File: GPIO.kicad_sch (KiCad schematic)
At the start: 18 parts, among them J11 74LS245, J9 uPD446, K15 74LS04, U2 74LS10

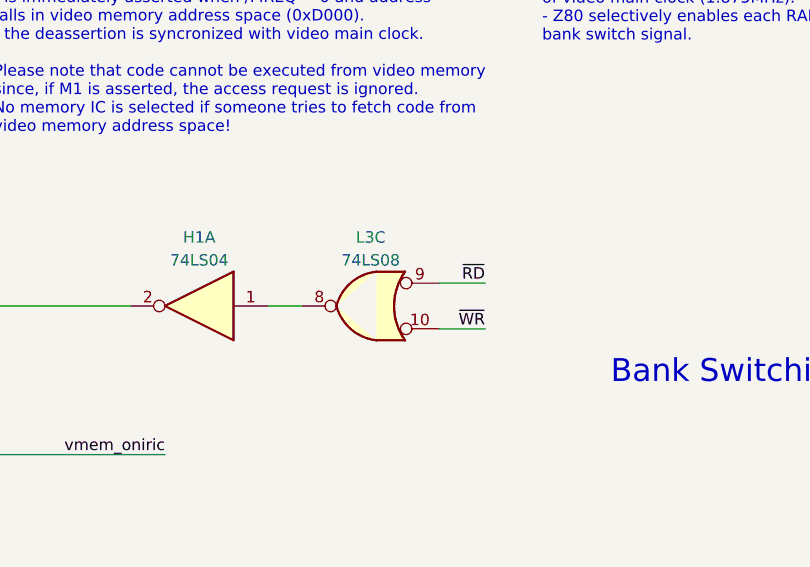
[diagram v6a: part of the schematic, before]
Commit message: IO addressing space multiplexing and small IO description
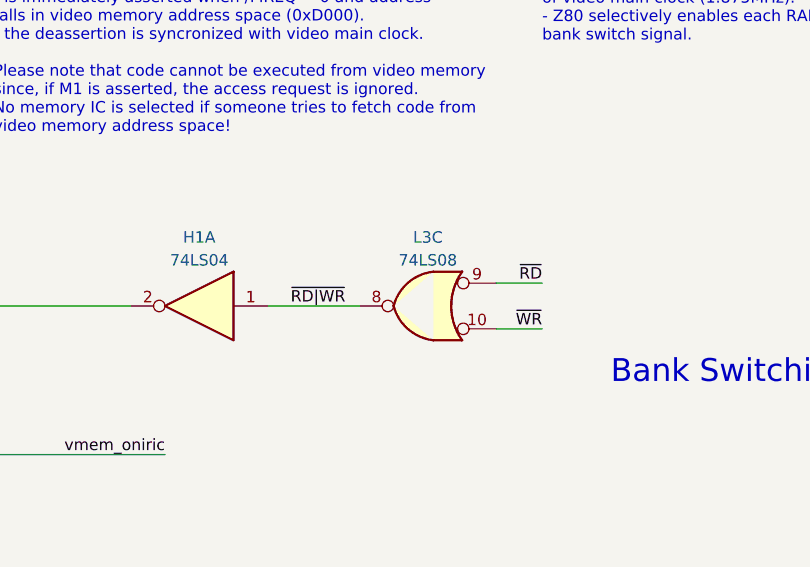
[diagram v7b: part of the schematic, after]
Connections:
- net ~{RD|WR}: now reaches H1.1, L3.8
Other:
- moved on the sheet: L3C
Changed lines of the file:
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@@
     (stroke (width 0) (type default))
   )
-  (wire (pts (xy 173.99 153.67) (xy 179.07 153.67))
+  (wire (pts (xy 180.34 153.67) (xy 185.42 153.67))
     (stroke (width 0) (type default))
   )
@@
     (stroke (width 0) (type default))
   )
-  (wire (pts (xy 173.99 148.59) (xy 179.07 148.59))
+  (wire (pts (xy 180.34 148.59) (xy 185.42 148.59))
     (stroke (width 0) (type default))
   )
@@
     (stroke (width 0) (type default))
   )
-  (wire (pts (xy 154.94 151.13) (xy 158.75 151.13))
+  (wire (pts (xy 154.94 151.13) (xy 165.1 151.13))
     (stroke (width 0) (type default))
   )
@@
     (effects (font (size 1.27 1.27)) (justify right bottom))
   )
-  (label "~{WR}" (at 179.07 153.67 180) (fields_autoplaced)
+  (label "~{WR}" (at 185.42 153.67 180) (fields_autoplaced)
     (effects (font (size 1.27 1.27)) (justify right bottom))
   )
@@
     (effects (font (size 1.27 1.27)) (justify left bottom))
   )
+  (label "~{RD|WR}" (at 157.48 151.13 0) (fields_autoplaced)
+    (effects (font (size 1.27 1.27)) (justify left bottom))
+  )
   (label "vmem_oniric" (at -19.05 274.32 0) (fields_autoplaced)
     (effects (font (size 1.27 1.27)) (justify left bottom))
@@
     (effects (font (size 1.27 1.27)) (justify left bottom))
   )
-  (label "~{RD}" (at 179.07 148.59 180) (fields_autoplaced)
+  (label "~{RD}" (at 185.42 148.59 180) (fields_autoplaced)
     (effects (font (size 1.27 1.27)) (justify right bottom))
   )
@@
     )
   )
-  (symbol (lib_id "74xx:74LS08") (at 166.37 151.13 0) (mirror y) (unit 3) (convert 2)
+  (symbol (lib_id "74xx:74LS08") (at 172.72 151.13 0) (mirror y) (unit 3) (convert 2)
     (in_bom yes) (on_board yes) (dnp no) (fields_autoplaced)
-    (property "Reference" "L3" (at 166.37 143.51 0)
+    (property "Reference" "L3" (at 172.72 143.51 0)
       (effects (font (size 1.27 1.27)))
     )
-    (property "Value" "74LS08" (at 166.37 146.05 0)
+    (property "Value" "74LS08" (at 172.72 146.05 0)
       (effects (font (size 1.27 1.27)))
     )
-    (property "Footprint" "" (at 166.37 151.13 0)
-      (effects (font (size 1.27 1.27)) hide)
-    )
-    (property "Datasheet" "http://www.ti.com/lit/gpn/sn74LS08" (at 166.37 151.13 0)
-      (effects (font (size 1.27 1.27)) hide)
-    )
+    (property "Footprint" "" (at 172.72 151.13 0)
+      (effects (font (size 1.27 1.27)) hide)
+    )
+    (property "Datasheet" "http://www.ti.com/lit/gpn/sn74LS08" (at 172.72 151.13 0)
+      (effects (font (size 1.27 1.27)) hide)
+    )

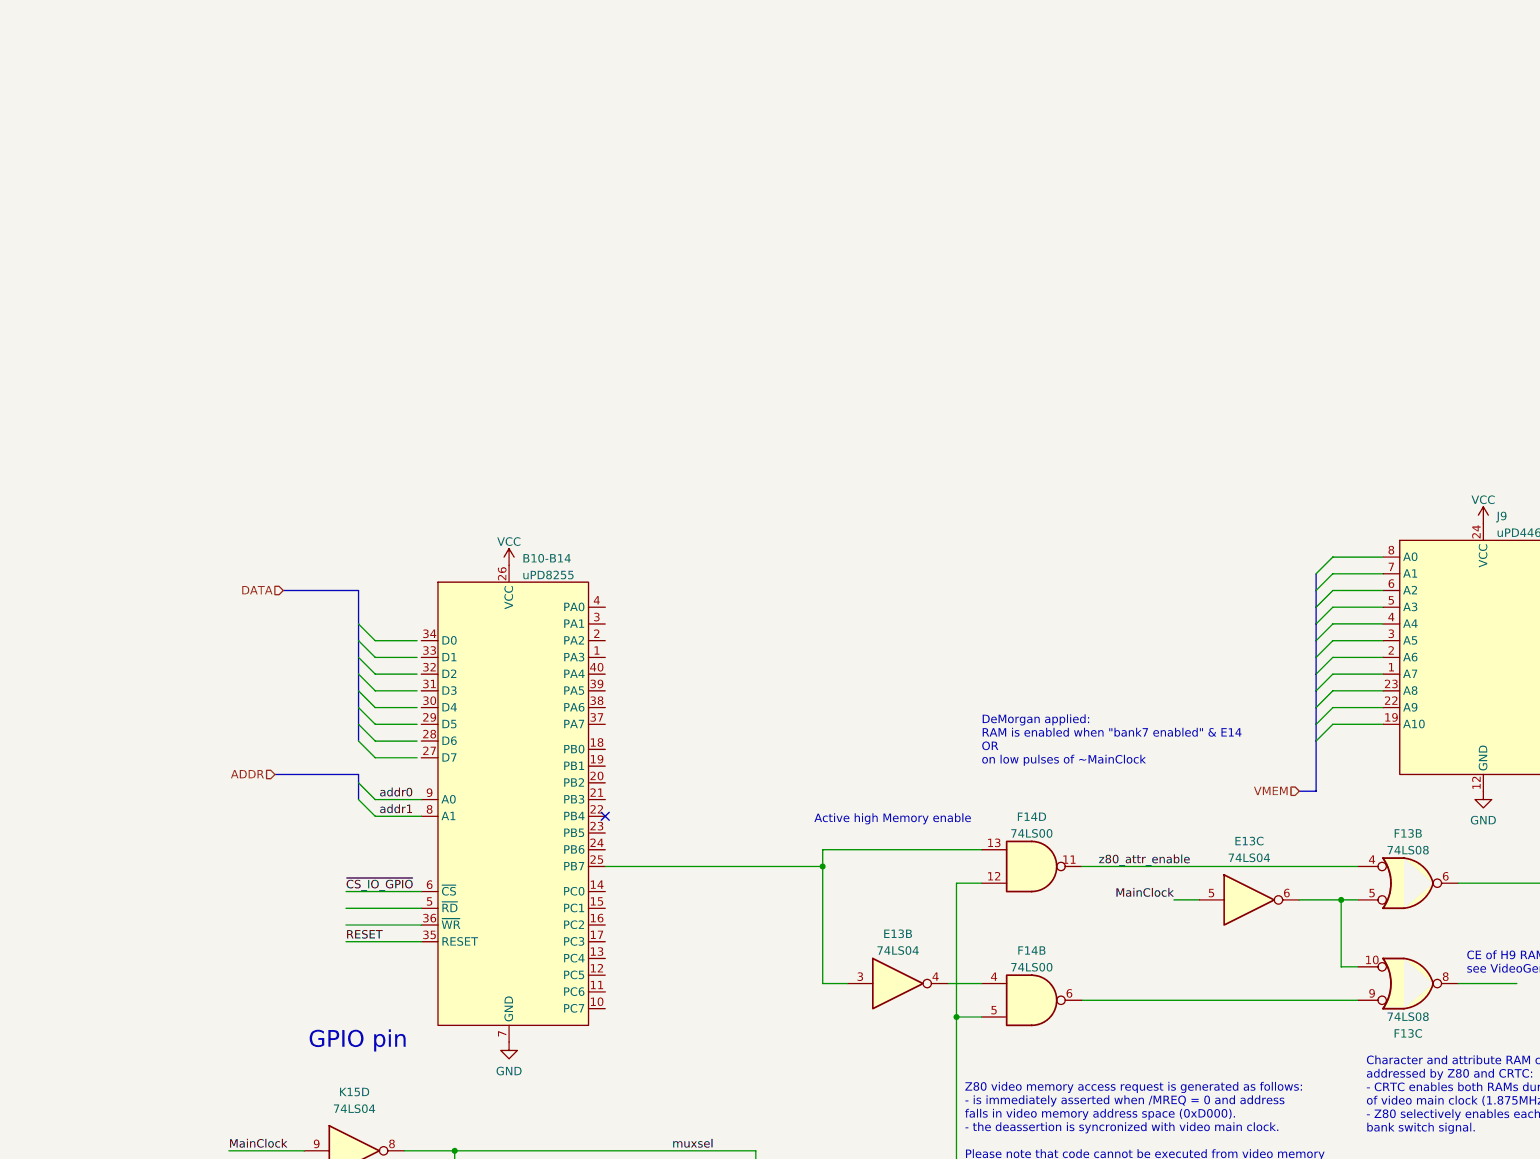
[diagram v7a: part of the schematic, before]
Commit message: Added FDC sheet (WIP), added partial parallel port inout
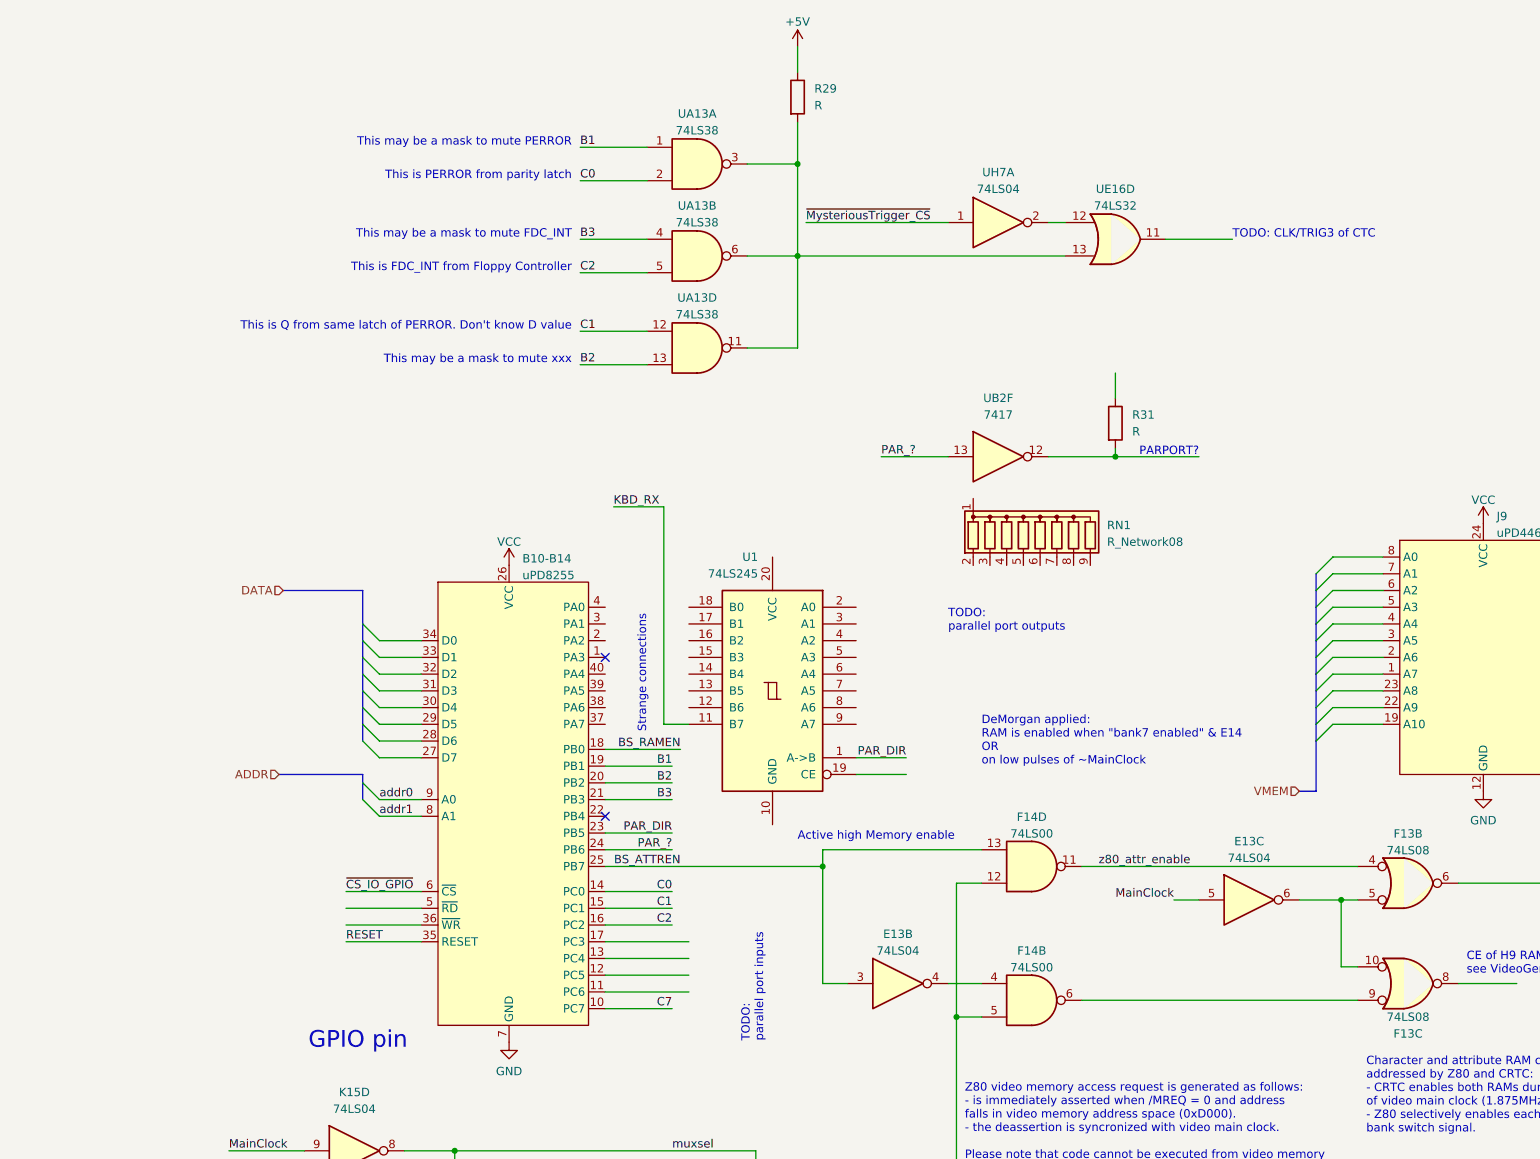
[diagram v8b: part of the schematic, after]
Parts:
- added R29, R31: R, symbol Device:R
- added RN1: R_Network08, Resistor_THT:R_Array_SIP9, symbol Device:R_Network08
- added U1: 74LS245, symbol 74xx:74LS245
- added UA13: 74LS38, symbol 74xx:74LS38
- added UB2: 7417, symbol 74xx:74LS04
- added UE16: 74LS32, symbol 74xx:74LS32
- added UH7: 74LS04, symbol 74xx:74LS04
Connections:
- net BS_ATTREN: now reaches B10-B14.25 (PB7), E13.3, F14.13
- net C7: now reaches B10-B14.10 (PC7)
- net C0: now reaches B10-B14.14 (PC0)
- net C0: now also UA13.2
- net C1: now reaches B10-B14.15 (PC1)
- net C1: now also UA13.12
- net C2: now reaches B10-B14.16 (PC2)
- net C2: now also UA13.5
- net BS_RAMEN: now reaches B10-B14.18 (PB0)
- net B1: now reaches B10-B14.19 (PB1)
- net B1: now also UA13.1
- net B2: now reaches B10-B14.20 (PB2)
- net B2: now also UA13.13
- net B3: now reaches B10-B14.21 (PB3)
- net B3: now also UA13.4
- net PAR_DIR: now reaches B10-B14.23 (PB5)
- net PAR_DIR: now also U1.1 (A->B)
- net PAR_?: now reaches B10-B14.24 (PB6)
- net PAR_?: now also UB2.13
- new net: UE16.12, UH7.2
- new net: R29.2, UA13.11, UA13.3, UA13.6, UE16.13
- new net: R31.2, UB2.12
- new net +5V: R29.1
- new net KBD_RX: U1.11 (B7)
- new net ~{MysteriousTrigger_CS}: UH7.1
- no-connect marks 1 -> 2
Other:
- note added: "PARPORT?"
- note added: "Strange connections"
- note added: "TODO: CLK/TRIG3 of CTC"
- note added: "TODO: parallel port inputs"
- note added: "TODO: parallel port outputs"
- note added: "This is FDC_INT from Floppy Controller"
- note added: "This is PERROR from parity latch"
- note added: "This is Q from same latch of PERROR. Don't know D value"
- note added: "This may be a mask to mute FDC_INT"
- note added: "This may be a mask to mute PERROR"
- note added: "This may be a mask to mute xxx"
